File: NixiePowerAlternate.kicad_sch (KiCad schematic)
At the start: 27 parts, among them J1 12VDC, J2 Screw_Terminal_01x02, J3 Screw_Terminal_01x03, J4 Screw_Terminal_01x03, U1 AMS1117-5.0, U2 MAX1771ESA, U3 AMS1117-3.3

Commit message: Add files via upload
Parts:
- removed RV1: 5K, Potentiometer_THT:Potentiometer_Bourns_3386P_Vertical, symbol Device:R_Potentiometer_Trim_US
- R1: renamed from R3; value 8.2K -> 10K; MPN 0805W8F8201T5E -> (none); Manufacturer UniRoyal -> (none)
- R2: value 1.2M -> 1,15M; LCSC C22107 -> C422602; Part# 1206W4F1204T5E -> 1206W4F1154T5E
- renumbered R1 to R3
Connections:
- net GND: now also R1.2
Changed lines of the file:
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@@
 (kicad_sch (version 20211123) (generator eeschema)
   (paper "A4")
-  (junction (at 170.18 80.01) (diameter 0) (color 0 0 0 0)
-  )
   (junction (at 125.73 113.03) (diameter 0) (color 0 0 0 0)
   )
@@
   (junction (at 157.48 40.64) (diameter 0) (color 0 0 0 0)
   )
-  (junction (at 173.99 75.946) (diameter 0) (color 0 0 0 0)
-  )
   (junction (at 171.45 113.03) (diameter 0) (color 0 0 0 0)
   )
@@
     (stroke (width 0) (type default) (color 0 0 0 0))
   )
-  (wire (pts (xy 170.18 79.756) (xy 170.18 80.01))
-    (stroke (width 0) (type default) (color 0 0 0 0))
-  )
   (wire (pts (xy 123.444 57.15) (xy 123.444 66.04))
     (stroke (width 0) (type default) (color 0 0 0 0))
@@
     (stroke (width 0) (type default) (color 0 0 0 0))
   )
-  (wire (pts (xy 173.99 80.01) (xy 170.18 80.01))
+  (wire (pts (xy 170.18 71.12) (xy 170.18 72.39))
     (stroke (width 0) (type default) (color 0 0 0 0))
   )
@@
     (stroke (width 0) (type default) (color 0 0 0 0))
   )
-  (wire (pts (xy 173.99 75.946) (xy 173.99 80.01))
-    (stroke (width 0) (type default) (color 0 0 0 0))
-  )
   (wire (pts (xy 158.75 120.65) (xy 158.75 124.46))
     (stroke (width 0) (type default) (color 0 0 0 0))
@@
     (stroke (width 0) (type default) (color 0 0 0 0))
   )
-  (wire (pts (xy 174.244 75.946) (xy 173.99 75.946))
-    (stroke (width 0) (type default) (color 0 0 0 0))
-  )
   (wire (pts (xy 88.138 66.04) (xy 85.344 66.04))
     (stroke (width 0) (type default) (color 0 0 0 0))
@@
   )
   (wire (pts (xy 137.668 40.64) (xy 137.668 46.99))
-    (stroke (width 0) (type default) (color 0 0 0 0))
-  )
-  (wire (pts (xy 170.18 71.12) (xy 170.18 72.136))
     (stroke (width 0) (type default) (color 0 0 0 0))
   )
@@
     (pin "8")
   )
-  (symbol (lib_id "Device:R_Potentiometer_Trim_US") (at 170.18 75.946 0) (unit 1)
-    (in_bom yes) (on_board yes) (fields_autoplaced)
-    (property "Reference" "RV1" (id 0) (at 168.529 75.1113 0)
-      (effects (font (size 1.27 1.27)) (justify right))
-    )
-    (property "Value" "5K" (id 1) (at 168.529 77.6482 0)
-      (effects (font (size 1.27 1.27)) (justify right))
-    )
-    (property "Footprint" "Potentiometer_THT:Potentiometer_Bourns_3386P_Vertical" (id 2) (at 170.18 75.946 0)
-      (effects (font (size 1.27 1.27)) hide)
-    )
-    (property "Datasheet" "~" (id 3) (at 170.18 75.946 0)
-      (effects (font (size 1.27 1.27)) hide)
-    )
-    (property "MPN" "3386P-1-502LF" (id 4) (at 170.18 75.946 0)
-      (effects (font (size 1.27 1.27)) hide)
-    )
-    (property "RSWWW" "522-2772" (id 5) (at 170.18 75.946 0)
-      (effects (font (size 1.27 1.27)) hide)
-    )
-    (pin "1")
-    (pin "2")
-    (pin "3")
-  )
   (symbol (lib_id "Device:C_Polarized_Small_US") (at 97.79 118.11 0) (unit 1)
     (in_bom yes) (on_board yes)
@@
   (symbol (lib_id "Device:R_Small_US") (at 157.48 68.58 0) (unit 1)
     (in_bom yes) (on_board yes)
-    (property "Reference" "R1" (id 0) (at 158.75 67.31 0)
+    (property "Reference" "R3" (id 0) (at 158.75 67.31 0)
       (effects (font (size 1.27 1.27)) (justify left))
     )
@@
   (symbol (lib_id "Device:R_Small_US") (at 170.18 68.58 0) (unit 1)
     (in_bom yes) (on_board yes)
-    (property "Reference" "R3" (id 0) (at 171.45 67.31 0)
-      (effects (font (size 1.27 1.27)) (justify left))
-    )
-    (property "Value" "8.2K" (id 1) (at 171.45 69.85 0)
+    (property "Reference" "R1" (id 0) (at 171.45 67.31 0)
+      (effects (font (size 1.27 1.27)) (justify left))
+    )
+    (property "Value" "10K" (id 1) (at 171.45 69.85 0)
       (effects (font (size 1.27 1.27)) (justify left))
     )
@@
       (effects (font (size 1.27 1.27)) hide)
     )
-    (property "Manufacturer" "UniRoyal" (id 4) (at 170.18 68.58 0)
-      (effects (font (size 1.27 1.27)) hide)
-    )
-    (property "MPN" "0805W8F8201T5E" (id 5) (at 170.18 68.58 0)
+    (property "Manufacturer" "" (id 4) (at 170.18 68.58 0)
+      (effects (font (size 1.27 1.27)) hide)
+    )
+    (property "MPN" "" (id 5) (at 170.18 68.58 0)
       (effects (font (size 1.27 1.27)) hide)
     )
@@
     (pin "2")
   )
-  (symbol (lib_id "power:GND") (at 170.18 80.01 0) (unit 1)
-    (in_bom yes) (on_board yes)
-    (property "Reference" "#PWR020" (id 0) (at 170.18 86.36 0)
-      (effects (font (size 1.27 1.27)) hide)
-    )
-    (property "Value" "GND" (id 1) (at 170.18 83.82 90)
+  (symbol (lib_id "power:GND") (at 170.18 72.39 0) (unit 1)
+    (in_bom yes) (on_board yes)
+    (property "Reference" "#PWR020" (id 0) (at 170.18 78.74 0)
+      (effects (font (size 1.27 1.27)) hide)
+    )
+    (property "Value" "GND" (id 1) (at 170.18 76.2 90)
       (effects (font (size 1.27 1.27)) (justify right))
     )
-    (property "Footprint" "" (id 2) (at 170.18 80.01 0)
-      (effects (font (size 1.27 1.27)) hide)
-    )
-    (property "Datasheet" "" (id 3) (at 170.18 80.01 0)
+    (property "Footprint" "" (id 2) (at 170.18 72.39 0)
+      (effects (font (size 1.27 1.27)) hide)
+    )
+    (property "Datasheet" "" (id 3) (at 170.18 72.39 0)
       (effects (font (size 1.27 1.27)) hide)
     )
@@
       (effects (font (size 1.27 1.27)) (justify left))
     )
-    (property "Value" "1.2M" (id 1) (at 171.45 53.34 0)
+    (property "Value" "1,15M" (id 1) (at 171.45 53.34 0)
       (effects (font (size 1.27 1.27)) (justify left))
     )
@@
       (effects (font (size 1.27 1.27)) hide)
     )
-    (property "Part#" "1206W4F1204T5E" (id 5) (at 170.18 52.07 0)
-      (effects (font (size 1.27 1.27)) hide)
-    )
-    (property "LCSC" "C22107" (id 6) (at 170.18 52.07 0)
+    (property "Part#" "1206W4F1154T5E" (id 5) (at 170.18 52.07 0)
+      (effects (font (size 1.27 1.27)) hide)
+    )
+    (property "LCSC" "C422602" (id 6) (at 170.18 52.07 0)
       (effects (font (size 1.27 1.27)) hide)
     )
@@
       (reference "Q1") (unit 1) (value "~") (footprint "Package_TO_SOT_SMD:TO-263-2")
     )
+    (path "/9a1629b4-387e-438d-90e1-ed4ee58c81af"
+      (reference "R1") (unit 1) (value "10K") (footprint "Resistor_SMD:R_0805_2012Metric_Pad1.20x1.40mm_HandSolder")
+    )
+    (path "/e65dcedd-ec8a-4128-b178-b566e74c1c46"
+      (reference "R2") (unit 1) (value "1,15M") (footprint "Resistor_SMD:R_1206_3216Metric_Pad1.30x1.75mm_HandSolder")
+    )
     (path "/8dbf8e23-256b-4644-8160-93c3e12988ca"
-      (reference "R1") (unit 1) (value "0.05") (footprint "Resistor_SMD:R_1206_3216Metric_Pad1.30x1.75mm_HandSolder")
-    )
-    (path "/e65dcedd-ec8a-4128-b178-b566e74c1c46"
-      (reference "R2") (unit 1) (value "1.2M") (footprint "Resistor_SMD:R_1206_3216Metric_Pad1.30x1.75mm_HandSolder")
-    )
-    (path "/9a1629b4-387e-438d-90e1-ed4ee58c81af"
-      (reference "R3") (unit 1) (value "8.2K") (footprint "Resistor_SMD:R_0805_2012Metric_Pad1.20x1.40mm_HandSolder")
-    )
-    (path "/330a9517-b917-4f23-ba10-dc98a671f631"
-      (reference "RV1") (unit 1) (value "5K") (footprint "Potentiometer_THT:Potentiometer_Bourns_3386P_Vertical")
+      (reference "R3") (unit 1) (value "0.05") (footprint "Resistor_SMD:R_1206_3216Metric_Pad1.30x1.75mm_HandSolder")
     )
     (path "/aa532763-7a77-49a3-9a10-76490ba21f14"

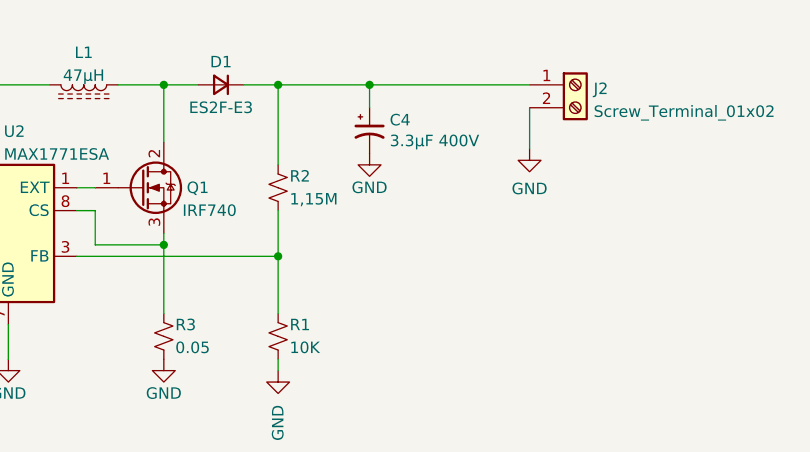
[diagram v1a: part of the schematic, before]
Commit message: Add files via upload
Checked L1 and Q1 against recommendations in the datasheet.  Decided to keep as is.  The MOSFET is fine.  L1 should be too and it is rated for 400V. 
Added feed forward capacitor C9, 47pF in parallel with R2.    The datasheet suggests values between 47pF and 220pF, using the lowest that insures stability.  The design is stable in PSPICE without the cap.  In practice it may be optional. 

Updated the PCB with the parts changes and fixed a layout error from Rev 0.
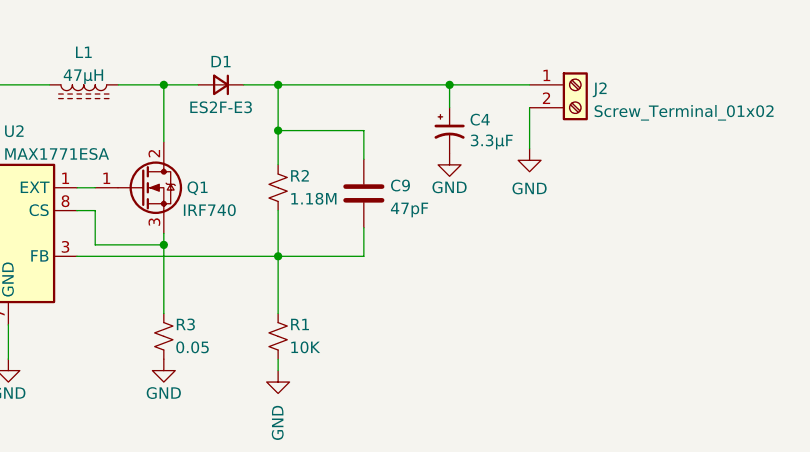
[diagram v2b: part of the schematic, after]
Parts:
- added C9: 47pF, Capacitor_SMD:C_1206_3216Metric_Pad1.33x1.80mm_HandSolder, symbol Device:C
- C4: value 3.3µF 400V -> 3.3µF
- L1: MPN (none) -> MSS1210H-473ME
- R2: value 1,15M -> 1.18M; LCSC C422602 -> C422598; Part# 1206W4F1154T5E -> 1206W4F1184T5E
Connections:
- net at R1.1, R2.2, U2.3 (FB): now also C9.2
- net at C4.1, D1.1 (K), J2.1 (Pin_1)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: now also C9.1
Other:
- moved on the sheet: C4
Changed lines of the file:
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@@
   (junction (at 121.92 40.64) (diameter 0) (color 0 0 0 0)
   )
+  (junction (at 170.18 45.72) (diameter 0) (color 0 0 0 0)
+  )
   (junction (at 171.45 111.76) (diameter 0) (color 0 0 0 0)
   )
@@
   (junction (at 110.49 40.64) (diameter 0) (color 0 0 0 0)
   )
+  (junction (at 189.23 40.64) (diameter 0) (color 0 0 0 0)
+  )
   (junction (at 97.79 40.64) (diameter 0) (color 0 0 0 0)
   )
-  (junction (at 180.34 40.64) (diameter 0) (color 0 0 0 0)
-  )
   (junction (at 123.444 66.04) (diameter 0) (color 0 0 0 0)
   )
@@
     (stroke (width 0) (type default) (color 0 0 0 0))
   )
-  (wire (pts (xy 180.34 40.64) (xy 198.12 40.64))
-    (stroke (width 0) (type default) (color 0 0 0 0))
-  )
   (wire (pts (xy 195.072 109.22) (xy 198.12 109.22))
     (stroke (width 0) (type default) (color 0 0 0 0))
@@
     (stroke (width 0) (type default) (color 0 0 0 0))
   )
-  (wire (pts (xy 170.18 40.64) (xy 170.18 49.53))
+  (wire (pts (xy 170.18 40.64) (xy 170.18 45.72))
+    (stroke (width 0) (type default) (color 0 0 0 0))
+  )
+  (wire (pts (xy 179.705 59.69) (xy 170.18 59.69))
     (stroke (width 0) (type default) (color 0 0 0 0))
   )
@@
     (stroke (width 0) (type default) (color 0 0 0 0))
   )
+  (wire (pts (xy 179.705 45.72) (xy 170.18 45.72))
+    (stroke (width 0) (type default) (color 0 0 0 0))
+  )
   (wire (pts (xy 121.92 40.64) (xy 110.49 40.64))
     (stroke (width 0) (type default) (color 0 0 0 0))
@@
     (stroke (width 0) (type default) (color 0 0 0 0))
   )
-  (wire (pts (xy 170.18 40.64) (xy 180.34 40.64))
-    (stroke (width 0) (type default) (color 0 0 0 0))
-  )
   (wire (pts (xy 113.03 120.65) (xy 113.03 124.46))
     (stroke (width 0) (type default) (color 0 0 0 0))
@@
     (stroke (width 0) (type default) (color 0 0 0 0))
   )
+  (wire (pts (xy 179.705 48.895) (xy 179.705 45.72))
+    (stroke (width 0) (type default) (color 0 0 0 0))
+  )
   (wire (pts (xy 127.508 57.15) (xy 123.444 57.15))
     (stroke (width 0) (type default) (color 0 0 0 0))
@@
     (stroke (width 0) (type default) (color 0 0 0 0))
   )
+  (wire (pts (xy 179.705 56.515) (xy 179.705 59.69))
+    (stroke (width 0) (type default) (color 0 0 0 0))
+  )
   (wire (pts (xy 170.18 59.69) (xy 170.18 66.04))
     (stroke (width 0) (type default) (color 0 0 0 0))
   )
+  (wire (pts (xy 189.23 40.64) (xy 198.12 40.64))
+    (stroke (width 0) (type default) (color 0 0 0 0))
+  )
   (wire (pts (xy 97.79 110.49) (xy 97.79 113.03))
     (stroke (width 0) (type default) (color 0 0 0 0))
@@
     (stroke (width 0) (type default) (color 0 0 0 0))
   )
+  (wire (pts (xy 170.18 40.64) (xy 189.23 40.64))
+    (stroke (width 0) (type default) (color 0 0 0 0))
+  )
   (wire (pts (xy 97.79 113.03) (xy 97.79 115.57))
     (stroke (width 0) (type default) (color 0 0 0 0))
@@
     (stroke (width 0) (type default) (color 0 0 0 0))
   )
-  (wire (pts (xy 180.34 40.64) (xy 180.34 43.18))
+  (wire (pts (xy 189.23 40.64) (xy 189.23 43.18))
     (stroke (width 0) (type default) (color 0 0 0 0))
   )
@@
   )
   (wire (pts (xy 140.208 67.31) (xy 140.208 71.12))
+    (stroke (width 0) (type default) (color 0 0 0 0))
+  )
+  (wire (pts (xy 170.18 45.72) (xy 170.18 49.53))
     (stroke (width 0) (type default) (color 0 0 0 0))
   )
@@
     (pin "1")
   )
-  (symbol (lib_id "Device:C_Polarized_Small_US") (at 180.34 45.72 0) (unit 1)
-    (in_bom yes) (on_board yes)
-    (property "Reference" "C4" (id 0) (at 182.5752 44.5516 0)
-      (effects (font (size 1.27 1.27)) (justify left))
-    )
-    (property "Value" "3.3µF 400V" (id 1) (at 182.5752 46.863 0)
-      (effects (font (size 1.27 1.27)) (justify left))
-    )
-    (property "Footprint" "Capacitor_THT:CP_Radial_D10.0mm_P5.00mm" (id 2) (at 180.34 45.72 0)
-      (effects (font (size 1.27 1.27)) hide)
-    )
-    (property "Datasheet" "~" (id 3) (at 180.34 45.72 0)
-      (effects (font (size 1.27 1.27)) hide)
-    )
-    (property "Manufacturer" "Nichicon" (id 4) (at 180.34 45.72 0)
-      (effects (font (size 1.27 1.27)) hide)
-    )
-    (property "Part#" "UPW2G3R3MPD" (id 5) (at 180.34 45.72 0)
+  (symbol (lib_id "Device:C_Polarized_Small_US") (at 189.23 45.72 0) (unit 1)
+    (in_bom yes) (on_board yes)
+    (property "Reference" "C4" (id 0) (at 191.4652 44.5516 0)
+      (effects (font (size 1.27 1.27)) (justify left))
+    )
+    (property "Value" "3.3µF" (id 1) (at 191.4652 46.863 0)
+      (effects (font (size 1.27 1.27)) (justify left))
+    )
+    (property "Footprint" "Capacitor_THT:CP_Radial_D10.0mm_P5.00mm" (id 2) (at 189.23 45.72 0)
+      (effects (font (size 1.27 1.27)) hide)
+    )
+    (property "Datasheet" "~" (id 3) (at 189.23 45.72 0)
+      (effects (font (size 1.27 1.27)) hide)
+    )
+    (property "Manufacturer" "Nichicon" (id 4) (at 189.23 45.72 0)
+      (effects (font (size 1.27 1.27)) hide)
+    )
+    (property "Part#" "UPW2G3R3MPD" (id 5) (at 189.23 45.72 0)
       (effects (font (size 1.27 1.27)) hide)
     )
@@
       (effects (font (size 1.27 1.27)) hide)
     )
-    (property "Datasheet" "~" (id 3) (at 148.59 40.64 0)
+    (property "Datasheet" "https://www.coilcraft.com/en-us/products/power/shielded-inductors/ferrite-drum/mss-mos/mss1210h/mss1210h-473/" (id 3) (at 148.59 40.64 0)
+      (effects (font (size 1.27 1.27)) hide)
+    )
+    (property "MPN" "MSS1210H-473ME" (id 4) (at 148.59 40.64 90)
       (effects (font (size 1.27 1.27)) hide)
     )
@@
     (pin "2")
   )
+  (symbol (lib_id "Device:C") (at 179.705 52.705 0) (unit 1)
+    (in_bom yes) (on_board yes) (fields_autoplaced)
+    (property "Reference" "C9" (id 0) (at 182.626 51.8703 0)
+      (effects (font (size 1.27 1.27)) (justify left))
+    )
+    (property "Value" "47pF" (id 1) (at 182.626 54.4072 0)
+      (effects (font (size 1.27 1.27)) (justify left))
+    )
+    (property "Footprint" "Capacitor_SMD:C_1206_3216Metric_Pad1.33x1.80mm_HandSolder" (id 2) (at 180.6702 56.515 0)
+      (effects (font (size 1.27 1.27)) hide)
+    )
+    (property "Datasheet" "~" (id 3) (at 179.705 52.705 0)
+      (effects (font (size 1.27 1.27)) hide)
+    )
+    (property "JLCPCB" "C113890" (id 4) (at 179.705 52.705 0)
+      (effects (font (size 1.27 1.27)) hide)
+    )
+    (property "MPN" "CC1206JRNPOBBN470" (id 5) (at 179.705 52.705 0)
+      (effects (font (size 1.27 1.27)) hide)
+    )
+    (pin "1")
+    (pin "2")
+  )
   (symbol (lib_id "power:GND") (at 170.18 72.39 0) (unit 1)
     (in_bom yes) (on_board yes)
@@
       (effects (font (size 1.27 1.27)) (justify left))
     )
-    (property "Value" "1,15M" (id 1) (at 171.45 53.34 0)
+    (property "Value" "1.18M" (id 1) (at 171.45 53.34 0)
       (effects (font (size 1.27 1.27)) (justify left))
     )
@@
       (effects (font (size 1.27 1.27)) hide)
     )
-    (property "Part#" "1206W4F1154T5E" (id 5) (at 170.18 52.07 0)
-      (effects (font (size 1.27 1.27)) hide)
-    )
-    (property "LCSC" "C422602" (id 6) (at 170.18 52.07 0)
+    (property "Part#" "1206W4F1184T5E" (id 5) (at 170.18 52.07 0)
+      (effects (font (size 1.27 1.27)) hide)
+    )
+    (property "LCSC" "C422598" (id 6) (at 170.18 52.07 0)
       (effects (font (size 1.27 1.27)) hide)
     )
@@
     (pin "1")
   )
-  (symbol (lib_id "power:GND") (at 180.34 48.26 0) (unit 1)
-    (in_bom yes) (on_board yes)
-    (property "Reference" "#PWR022" (id 0) (at 180.34 54.61 0)
-      (effects (font (size 1.27 1.27)) hide)
-    )
-    (property "Value" "GND" (id 1) (at 180.34 52.07 0))
-    (property "Footprint" "" (id 2) (at 180.34 48.26 0)
-      (effects (font (size 1.27 1.27)) hide)
-    )
-    (property "Datasheet" "" (id 3) (at 180.34 48.26 0)
+  (symbol (lib_id "power:GND") (at 189.23 48.26 0) (unit 1)
+    (in_bom yes) (on_board yes)
+    (property "Reference" "#PWR022" (id 0) (at 189.23 54.61 0)
+      (effects (font (size 1.27 1.27)) hide)
+    )
+    (property "Value" "GND" (id 1) (at 189.23 52.07 0))
+    (property "Footprint" "" (id 2) (at 189.23 48.26 0)
+      (effects (font (size 1.27 1.27)) hide)
+    )
+    (property "Datasheet" "" (id 3) (at 189.23 48.26 0)
       (effects (font (size 1.27 1.27)) hide)
     )
@@
     )
     (path "/5c54e8fb-9130-4d13-b141-e3402ceea36d"
-      (reference "C4") (unit 1) (value "3.3µF 400V") (footprint "Capacitor_THT:CP_Radial_D10.0mm_P5.00mm")
+      (reference "C4") (unit 1) (value "3.3µF") (footprint "Capacitor_THT:CP_Radial_D10.0mm_P5.00mm")
     )
     (path "/331f846c-b408-41df-8acc-5399e787fadb"
@@
       (reference "C8") (unit 1) (value "10uF") (footprint "Capacitor_Tantalum_SMD:CP_EIA-3216-18_Kemet-A")
     )
+    (path "/e59da0be-6556-473f-bc60-18952b549ffd"
+      (reference "C9") (unit 1) (value "47pF") (footprint "Capacitor_SMD:C_1206_3216Metric_Pad1.33x1.80mm_HandSolder")
+    )
     (path "/b1f04359-6e24-4a92-9d27-0dc0766087e6"
       (reference "D1") (unit 1) (value "~") (footprint "Diode_SMD:D_SMB")
@@
     )
     (path "/e65dcedd-ec8a-4128-b178-b566e74c1c46"
-      (reference "R2") (unit 1) (value "1,15M") (footprint "Resistor_SMD:R_1206_3216Metric_Pad1.30x1.75mm_HandSolder")
+      (reference "R2") (unit 1) (value "1.18M") (footprint "Resistor_SMD:R_1206_3216Metric_Pad1.30x1.75mm_HandSolder")
     )
     (path "/8dbf8e23-256b-4644-8160-93c3e12988ca"

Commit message: Add files via upload
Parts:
- removed C5: 1uF, Capacitor_SMD:C_0805_2012Metric_Pad1.18x1.45mm_HandSolder, symbol Device:C_Polarized_Small_US
- removed U1: AMS1117-5.0, Package_TO_SOT_SMD:SOT-223-3_TabPin2, symbol Regulator_Linear:AMS1117-5.0
- added C10, C11: 4.7uF, Capacitor_SMD:C_1206_3216Metric_Pad1.33x1.80mm_HandSolder, symbol Device:C
- added C12: 10nF, Capacitor_SMD:C_0805_2012Metric_Pad1.18x1.45mm_HandSolder, symbol Device:C
- added C13: 100uF, Capacitor_Tantalum_SMD:CP_EIA-3528-15_AVX-H_Pad1.50x2.35mm_HandSolder, symbol Device:C_Polarized_Small_US
- added C5: 4.7uF, symbol Device:C
- added D2: SS14FL, symbol Device:D_Schottky
- added L2: 47uH, symbol Device:L_Ferrite
- added R4: 10K, Resistor_SMD:R_0805_2012Metric_Pad1.20x1.40mm_HandSolder, symbol Device:R_US
- added R5: 3.24K, Resistor_SMD:R_0805_2012Metric_Pad1.20x1.40mm_HandSolder, symbol Device:R_US
- added U1: TPS5430DDA, Package_SO:TI_SO-PowerPAD-8_ThermalVias, symbol Regulator_Switching:TPS5430DDA
- C8: value 10uF -> 100uF; footprint Capacitor_Tantalum_SMD:CP_EIA-3216-18_Kemet-A -> Capacitor_Tantalum_SMD:CP_EIA-3528-15_AVX-H_Pad1.50x2.35mm_HandSolder; LCSC C7171 -> C16133; MPN TAJA106K016RNJ -> TAJB107K006RNJ; Manufacturer Kemet -> Kyocera AVX
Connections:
- net +12V: now also C10.1, C11.1, C5.1, U1.7 (VIN); no longer C6.1, U3.3 (VI)
- net +5V: now also C6.1, U3.3 (VI), C13.1, L2.2, R4.1
- net GND: now also C10.2, C11.2, C13.2, C5.2, D2.2 (A), R5.2, U1.6 (GND), U1.9 (GNDPAD)
- new net: R4.2, R5.1, U1.4 (VSENSE)
- new net: C12.1, U1.1 (BOOT)
- new net: C12.2, D2.1 (K), L2.1, U1.8 (PH)
- no-connect marks 0 -> 1
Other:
- moved on the sheet: C6, C7, C8, GND1, J1, J3, J4, U3

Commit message: Add files via upload
Replace linear 5V regulator with a buck SMPS in the schematic. 
Begin adding MSS1048 footprint
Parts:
- C5: footprint (none) -> Capacitor_SMD:C_1206_3216Metric_Pad1.33x1.80mm_HandSolder
- D2: footprint (none) -> Diode_SMD:D_SOD-123F
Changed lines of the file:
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@@
   (symbol (lib_id "power:+12V") (at 97.79 82.55 0) (unit 1)
     (in_bom yes) (on_board yes) (fields_autoplaced)
-    (property "Reference" "#PWR?" (id 0) (at 97.79 86.36 0)
+    (property "Reference" "#PWR0108" (id 0) (at 97.79 86.36 0)
       (effects (font (size 1.27 1.27)) hide)
     )
@@
       (effects (font (size 1.27 1.27)) (justify left))
     )
-    (property "Footprint" "" (id 2) (at 91.1352 123.19 0)
+    (property "Footprint" "Capacitor_SMD:C_1206_3216Metric_Pad1.33x1.80mm_HandSolder" (id 2) (at 91.1352 123.19 0)
       (effects (font (size 1.27 1.27)) hide)
     )
@@
       (effects (font (size 1.27 1.27)) (justify left))
     )
-    (property "Footprint" "" (id 2) (at 171.45 118.11 0)
+    (property "Footprint" "Diode_SMD:D_SOD-123F" (id 2) (at 171.45 118.11 0)
       (effects (font (size 1.27 1.27)) hide)
     )
@@
     )
     (path "/33b1ee0e-5887-4ef2-976a-e09dd11a4326"
-      (reference "#PWR?") (unit 1) (value "+12V") (footprint "")
+      (reference "#PWR0108") (unit 1) (value "+12V") (footprint "")
     )
     (path "/41612ed4-206d-4dd2-ac73-56b24c4ca740"
@@
     )
     (path "/7ad46cc4-3318-4374-810a-aff6cd741e9c"
-      (reference "C5") (unit 1) (value "4.7uF") (footprint "")
+      (reference "C5") (unit 1) (value "4.7uF") (footprint "Capacitor_SMD:C_1206_3216Metric_Pad1.33x1.80mm_HandSolder")
     )
     (path "/d125a2a5-cd1e-468e-81d5-207f1c1c1d1c"
@@
     )
     (path "/d32c5515-46f6-4e72-a33f-5545f7212eb8"
-      (reference "D2") (unit 1) (value "SS14FL") (footprint "")
+      (reference "D2") (unit 1) (value "SS14FL") (footprint "Diode_SMD:D_SOD-123F")
     )
     (path "/d16fc6b2-16ae-4841-bb38-af2a49ce6a1a"
